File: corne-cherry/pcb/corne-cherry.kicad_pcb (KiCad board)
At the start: 2 copper layers, 275.5 x 105.6 mm, 172 parts, among them J1 MJ-4PP-9, J2 OLED, J3 MJ-4PP-9, J4 OLED, SW1 SW_PUSH, SW10 SW_PUSH, SW11 SW_PUSH, SW12 SW_PUSH, SW13 SW_PUSH, SW14 SW_PUSH, SW15 SW_PUSH, SW16 SW_PUSH, SW17 SW_PUSH, SW18 SW_PUSH, SW19 SW_PUSH, SW2 SW_PUSH, SW20 SW_PUSH, SW21 SW_PUSH, SW22 SW_PUSH, SW23 SW_PUSH, SW24 SW_PUSH, SW25 SW_PUSH, SW26 SW_PUSH, SW27 SW_PUSH, SW28 SW_PUSH, SW29 SW_PUSH, SW3 SW_PUSH, SW30 SW_PUSH, SW31 SW_PUSH, SW32 SW_PUSH, SW33 SW_PUSH, SW34 SW_PUSH, SW35 SW_PUSH, SW36 SW_PUSH, SW37 SW_PUSH, SW38 SW_PUSH, SW39 SW_PUSH, SW4 SW_PUSH, SW40 SW_PUSH, SW41 SW_PUSH, SW42 SW_PUSH, SW5 SW_PUSH, SW6 SW_PUSH, SW7 SW_PUSH, SW8 SW_PUSH, SW9 SW_PUSH, U1 ProMicro, U2 ProMicro

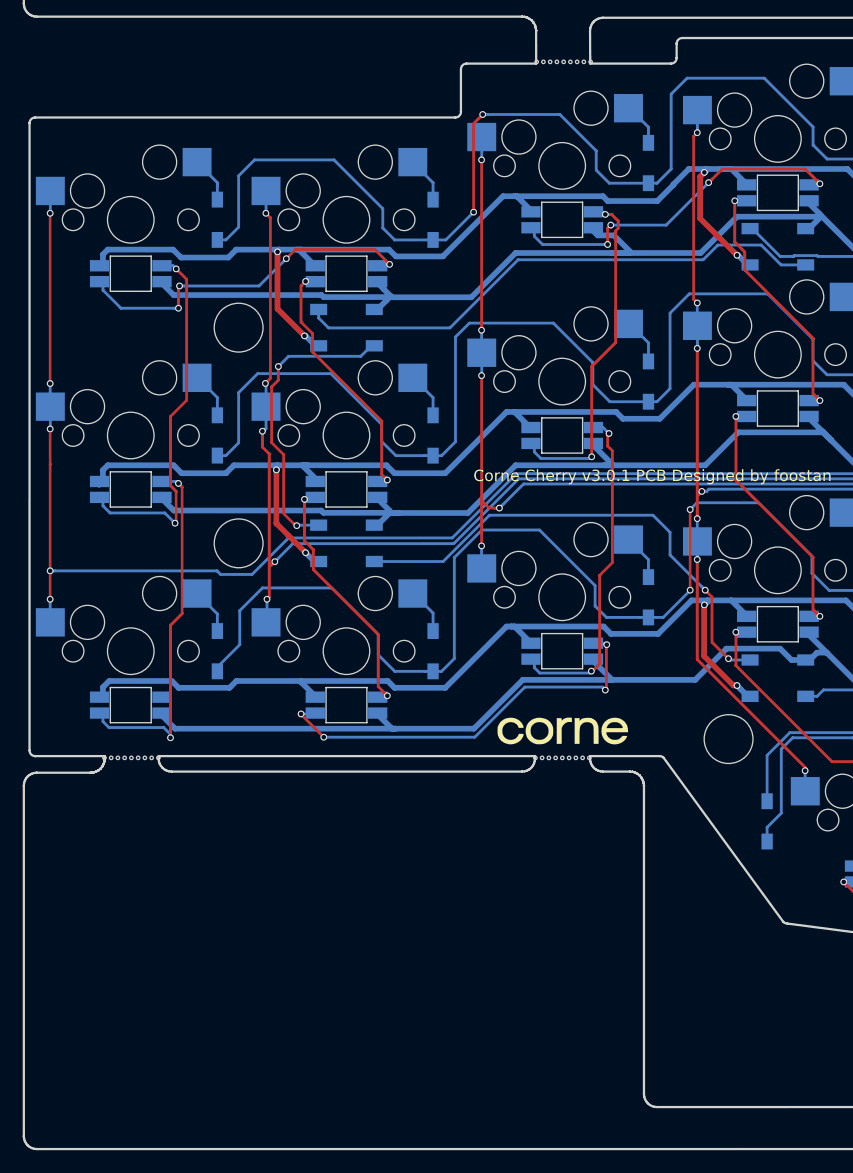
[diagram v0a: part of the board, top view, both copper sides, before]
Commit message: More column stagger
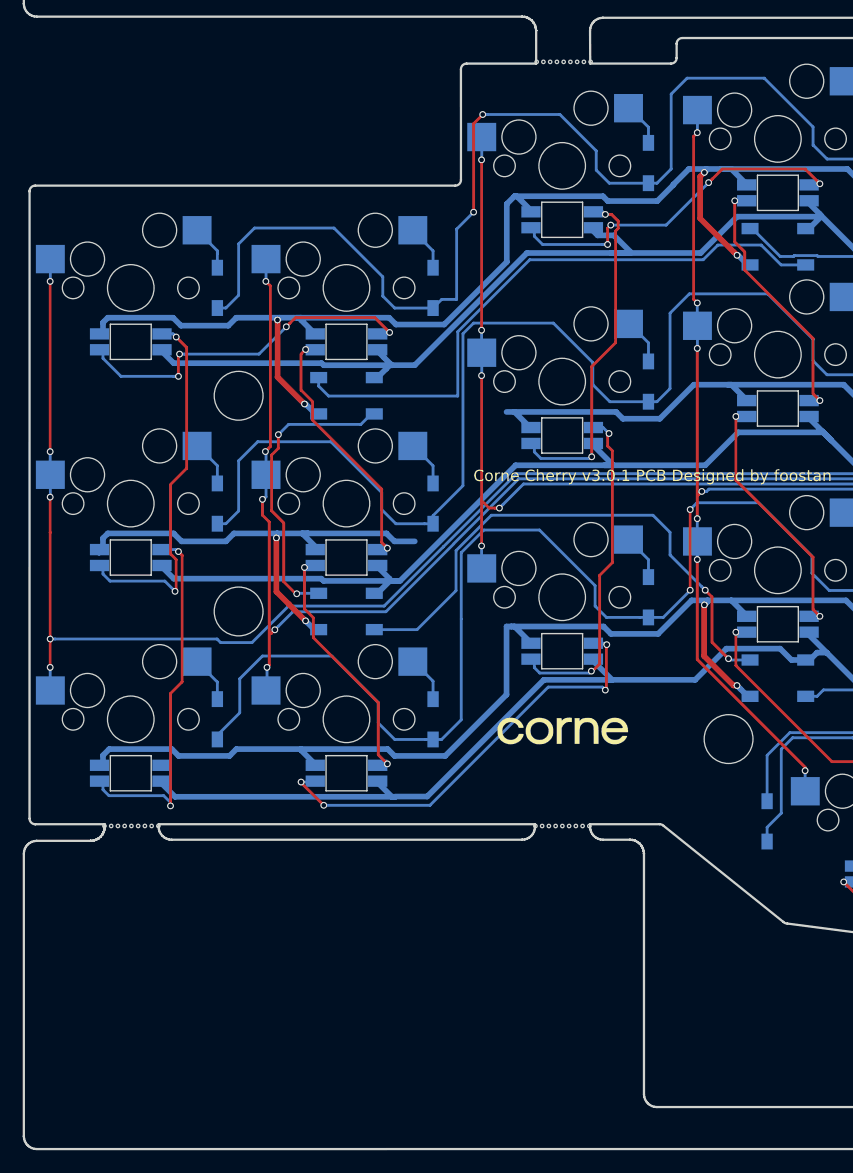
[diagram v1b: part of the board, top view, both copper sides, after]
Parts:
- moved D1 6.00 mm to (27.7, 41.8)
- moved D13 6.00 mm to (27.7, 79.8)
- moved D14 6.00 mm to (46.7, 79.8)
- moved D2 6.00 mm to (46.7, 41.8)
- moved D7 6.00 mm to (27.7, 60.8)
- moved D8 6.00 mm to (46.7, 60.8)
- moved LED1 6.00 mm to (39.1, 51.3)
- moved LED13 6.00 mm to (20.1, 65.5)
- moved LED14 6.00 mm to (39.1, 65.5)
- moved LED19 6.00 mm to (20.1, 84.5)
- moved LED20 6.00 mm to (39.1, 84.5)
- moved LED4 6.00 mm to (39.1, 70.3)
- moved LED7 6.00 mm to (20.1, 46.5)
- moved LED8 6.00 mm to (39.1, 46.5)
- moved REF** 6.00 mm to (58.1, 89.2)
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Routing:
- net VCC: track 544.3 -> 551.7 mm
- net row0: track 183.2 -> 189.3 mm
- net row2: track 180.7 -> 186.6 mm
- net Net-(LED1-Pad4): track 47.8 -> 53.6 mm
- net row1: track 193.3 -> 198.7 mm
- net Net-(LED4-Pad2): track 43.6 -> 48.1 mm
- net col0: track 170.3 -> 172.8 mm
- net Net-(LED20-Pad4): track 36.8 -> 39.3 mm
- net col1: track 149.4 -> 151.9 mm
- net GND: track 637.2 -> 638.3 mm
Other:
- outline, holes or cut-outs redrawn
